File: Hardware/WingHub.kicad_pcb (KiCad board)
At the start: 2 copper layers, 50.8 x 22.9 mm, 19 parts, among them J1 feather long, J2 feather short, J3 USB_A, SW2 DOWNLOADER, U1 CH559T

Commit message: add model USB 3D
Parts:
- removed the J3 at (39.1, 33.3) (x2)
- removed the SW2 at (66.0, 33.3) (x2)
- added J3 (x2): USB_A, Connector_USB:USB_A_CONNFLY_DS1095-WNR0, F.Cu at (39.1, 33.3)
- added SW2 (x2): DOWNLOADER, Button_Switch_SMD:SW_SPST_TL3342, F.Cu at (66.0, 33.3)
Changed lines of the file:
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@@
     (tracks 182)
     (zones 0)
-    (modules 17)
+    (modules 19)
     (nets 42)
   )
@@
     (pad 5 thru_hole circle (at 10.07 2.71 270) (size 3.5 3.5) (drill 2.3) (layers *.Cu *.Mask)
       (net 6 "Net-(J3-Pad5)"))
-    (model ${KISYS3DMOD}/Connector_USB.3dshapes/USB_A_CONNFLY_DS1095-WNR0.wrl
-      (at (xyz 0 0 0))
+    (model ${KIPRJMOD}/femaleThruHoleUSB.stp
+      (offset (xyz 3.5 -12.5 4))
       (scale (xyz 1 1 1))
       (rotate (xyz 0 0 0))

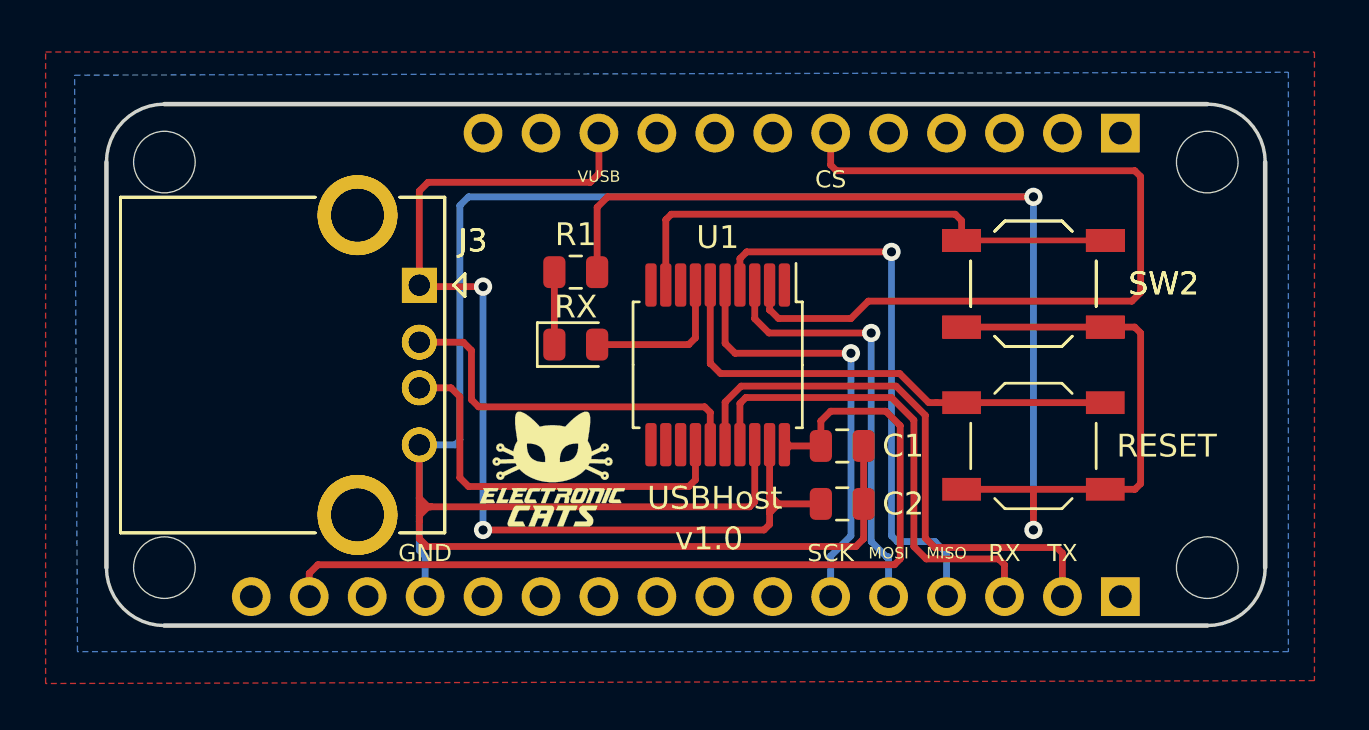
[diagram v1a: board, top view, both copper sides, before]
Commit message: fix labels pinout
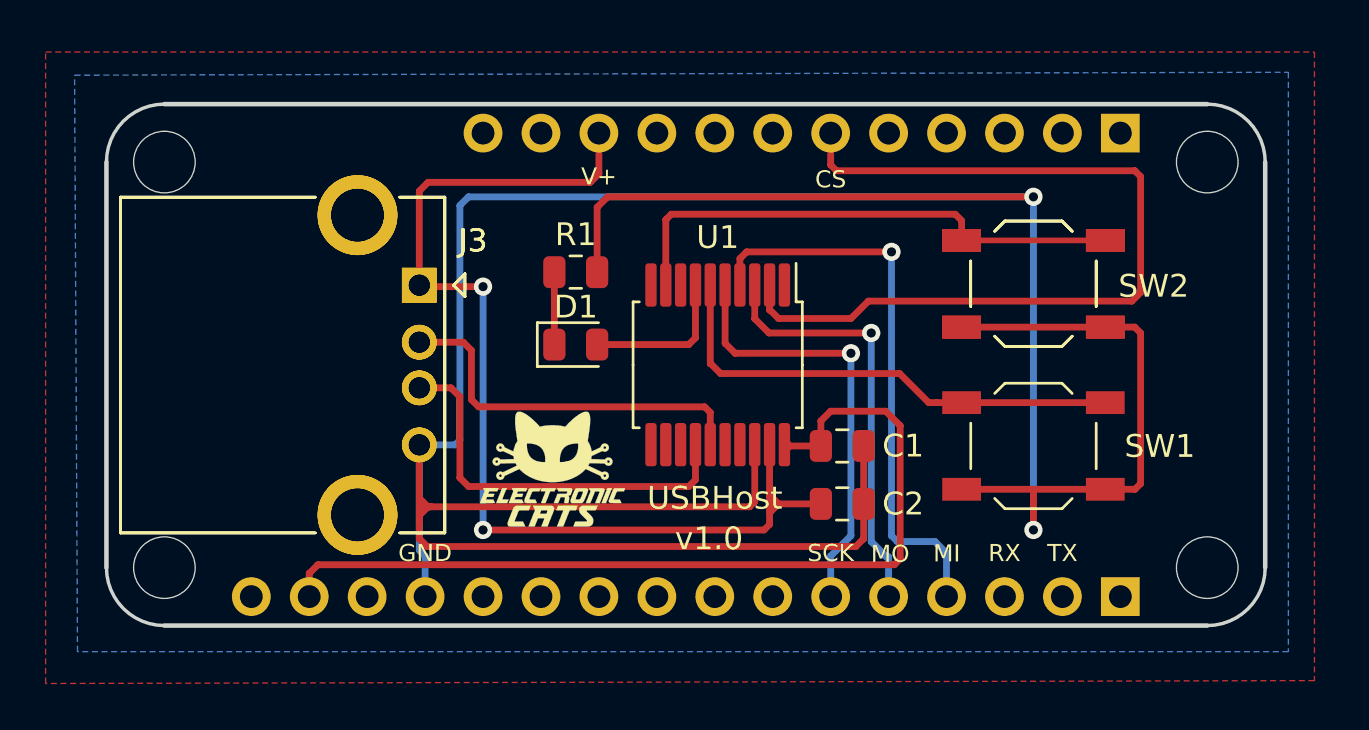
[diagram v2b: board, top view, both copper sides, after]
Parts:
- removed the J3 at (39.1, 33.3) (x2)
- removed the SW2 at (66.0, 33.3) (x2)
- added J3 (x2): USB_A, Connector_USB:USB_A_CONNFLY_DS1095-WNR0, F.Cu at (39.1, 33.3)
- added SW2 (x2): DOWNLOADER, Button_Switch_SMD:SW_SPST_TL3342, F.Cu at (66.0, 33.3)
- renumbered RX to D1, RESET to SW1
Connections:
- U1 pad 16: /TX -> /RX
- U1 pad 17: /RX -> /TX
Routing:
- net /TX: track 25.1 -> 0.00 mm
- net /RX: track 21.2 -> 0.00 mm
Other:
- board text added: "MI"
- board text added: "MO"
- board text added: "V+"
- board text removed: "MISO"
- board text removed: "MOSI"
- board text removed: "VUSB"
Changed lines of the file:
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@@
     (thickness 1.6)
     (drawings 25)
-    (tracks 182)
+    (tracks 162)
     (zones 0)
     (modules 19)
@@
     (38 B.Mask user)
     (39 F.Mask user)
-    (40 Dwgs.User user hide)
+    (40 Dwgs.User user)
     (41 Cmts.User user)
     (42 Eco1.User user)
@@
     (46 B.CrtYd user)
     (47 F.CrtYd user)
-    (48 B.Fab user hide)
-    (49 F.Fab user hide)
+    (48 B.Fab user)
+    (49 F.Fab user)
   )
   (setup
@@
     (tags "SPST Tactile Switch")
     (attr smd)
-    (fp_text reference SW2 (at 5.715 0 180) (layer F.SilkS)
+    (fp_text reference SW2 (at 5.27 0.106 180) (layer F.SilkS)
       (effects (font (size 1 1) (thickness 0.15)))
     )
@@
     (tags diode)
     (attr smd)
-    (fp_text reference RX (at 0 -1.65) (layer F.SilkS)
+    (fp_text reference D1 (at 0 -1.65) (layer F.SilkS)
       (effects (font (size 1 1) (thickness 0.15)))
     )
@@
       (net 3 GND))
     (pad 17 smd roundrect (at 3.5 -0.975 270) (size 1.9 0.5) (layers F.Cu F.Paste F.Mask) (roundrect_rratio 0.25)
+      (net 1 /TX))
+    (pad 16 smd roundrect (at 3.5 -0.325 270) (size 1.9 0.5) (layers F.Cu F.Paste F.Mask) (roundrect_rratio 0.25)
       (net 2 /RX))
-    (pad 16 smd roundrect (at 3.5 -0.325 270) (size 1.9 0.5) (layers F.Cu F.Paste F.Mask) (roundrect_rratio 0.25)
-      (net 1 /TX))
     (pad 15 smd roundrect (at 3.5 0.325 270) (size 1.9 0.5) (layers F.Cu F.Paste F.Mask) (roundrect_rratio 0.25)
       (net 33 /D-))
@@
     (tags "SPST Tactile Switch")
     (attr smd)
-    (fp_text reference SW2 (at 5.715 0 180) (layer F.SilkS)
+    (fp_text reference SW2 (at 6.39 -1.274 180) (layer F.Fab)
       (effects (font (size 1 1) (thickness 0.15)))
     )
@@
     (tags "SPST Tactile Switch")
     (attr smd)
-    (fp_text reference RESET (at 5.842 0 180) (layer F.SilkS)
+    (fp_text reference SW1 (at 5.54 0.014 180) (layer F.SilkS)
       (effects (font (size 1 1) (thickness 0.15)))
     )
@@
   (gr_line (start 55.88 22.86) (end 55.88 50.8) (layer F.Fab) (width 0.15))
   (gr_line (start 18.415 36.83) (end 80.01 36.83) (layer F.Fab) (width 0.15))
-  (gr_text VUSB (at 46.99 28.575) (layer F.SilkS)
-    (effects (font (size 0.5 0.5) (thickness 0.1)))
+  (gr_text V+ (at 46.99 28.575) (layer F.SilkS)
+    (effects (font (size 0.75 0.75) (thickness 0.15)))
   )
   (gr_text TX (at 67.31 45.085) (layer F.SilkS)
@@
     (effects (font (size 0.75 0.75) (thickness 0.15)))
   )
-  (gr_text MISO (at 62.23 45.085) (layer F.SilkS)
-    (effects (font (size 0.5 0.5) (thickness 0.1)))
-  )
-  (gr_text MOSI (at 59.69 45.085) (layer F.SilkS)
-    (effects (font (size 0.5 0.5) (thickness 0.1)))
+  (gr_text MI (at 62.24 45.1) (layer F.SilkS)
+    (effects (font (size 0.75 0.75) (thickness 0.15)))
+  )
+  (gr_text MO (at 59.76 45.12) (layer F.SilkS)
+    (effects (font (size 0.75 0.75) (thickness 0.15)))
   )
   (gr_text SCK (at 57.15 45.085) (layer F.SilkS)
@@
   (gr_line (start 76.2 27.94) (end 76.2 45.72) (layer Edge.Cuts) (width 0.2))
   (gr_line (start 27.94 25.4) (end 73.66 25.4) (layer Edge.Cuts) (width 0.2))
-  (segment (start 52.59699 40.25501) (end 52.522 40.33) (width 0.25) (layer F.Cu) (net 1))
-  (segment (start 67.31 45.212) (end 67.31 46.99) (width 0.3) (layer F.Cu) (net 1))
-  (segment (start 67.31 45.085) (end 67.31 45.212) (width 0.3) (layer F.Cu) (net 1))
-  (segment (start 61.71401 44.83899) (end 67.06399 44.83899) (width 0.3) (layer F.Cu) (net 1))
-  (segment (start 52.522 40.33) (end 52.522 38.46488) (width 0.3) (layer F.Cu) (net 1))
-  (segment (start 53.2249 37.76198) (end 60.018642 37.76198) (width 0.3) (layer F.Cu) (net 1))
-  (segment (start 67.06399 44.83899) (end 67.31 45.085) (width 0.3) (layer F.Cu) (net 1))
-  (segment (start 60.018642 37.76198) (end 61.298018 39.041358) (width 0.3) (layer F.Cu) (net 1))
-  (segment (start 52.522 38.46488) (end 53.2249 37.76198) (width 0.3) (layer F.Cu) (net 1))
-  (segment (start 61.298018 39.041358) (end 61.298018 44.422998) (width 0.3) (layer F.Cu) (net 1))
-  (segment (start 61.298018 44.422998) (end 61.71401 44.83899) (width 0.3) (layer F.Cu) (net 1))
-  (segment (start 64.77 45.593) (end 64.77 46.99) (width 0.3) (layer F.Cu) (net 2))
-  (segment (start 64.516 45.339) (end 64.77 45.593) (width 0.3) (layer F.Cu) (net 2))
-  (segment (start 61.341 45.339) (end 64.516 45.339) (width 0.3) (layer F.Cu) (net 2))
-  (segment (start 53.172 40.33) (end 53.172 38.522) (width 0.3) (layer F.Cu) (net 2))
-  (segment (start 53.172 38.522) (end 53.43201 38.26199) (width 0.3) (layer F.Cu) (net 2))
-  (segment (start 60.79801 44.79601) (end 61.341 45.339) (width 0.3) (layer F.Cu) (net 2))
-  (segment (start 53.43201 38.26199) (end 59.811532 38.26199) (width 0.3) (layer F.Cu) (net 2))
-  (segment (start 59.811532 38.26199) (end 60.798009 39.248467) (width 0.3) (layer F.Cu) (net 2))
-  (segment (start 60.798009 39.248467) (end 60.79801 44.79601) (width 0.3) (layer F.Cu) (net 2))
   (segment (start 39.116 46.736) (end 39.37 46.99) (width 0.5) (layer B.Cu) (net 3))
   (segment (start 58.5955 40.386) (end 58.5955 42.418) (width 0.3) (layer F.Cu) (net 3))
@@
     (connect_pads (clearance 0.508))
     (min_thickness 0.254)
-    (fill yes (arc_segments 32) (thermal_gap 0.508) (thermal_bridge_width 0.508))
+    (fill (arc_segments 32) (thermal_gap 0.508) (thermal_bridge_width 0.508))
     (polygon
       (pts
@@
     (connect_pads (clearance 0.508))
     (min_thickness 0.254)
-    (fill yes (arc_segments 32) (thermal_gap 0.508) (thermal_bridge_width 0.508))
+    (fill (arc_segments 32) (thermal_gap 0.508) (thermal_bridge_width 0.508))
     (polygon
       (pts

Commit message: Tx and Rx routes exchanged.
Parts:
- removed the J3 at (39.1, 33.3) (x2)
- removed the SW2 at (66.0, 33.3) (x2)
- added J3 (x2): USB_A, Connector_USB:USB_A_CONNFLY_DS1095-WNR0, F.Cu at (39.1, 33.3)
- added SW2 (x2): DOWNLOADER, Button_Switch_SMD:SW_SPST_TL3342, F.Cu at (66.0, 33.3)
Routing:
- net /RX: track 0.00 -> 23.8 mm
- net /TX: track 0.00 -> 23.6 mm, vias 0 -> 1

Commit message: labels buttons
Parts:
- removed the J3 at (39.1, 33.3) (x2)
- removed the SW2 at (66.0, 33.3) (x2)
- added J3 (x2): USB_A, Connector_USB:USB_A_CONNFLY_DS1095-WNR0, F.Cu at (39.1, 33.3)
- added PROG, SW2: DOWNLOADER, Button_Switch_SMD:SW_SPST_TL3342, F.Cu at (66.0, 33.3)
- renumbered SW1 to RESET
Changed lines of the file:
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@@
-(kicad_pcb (version 20171130) (host pcbnew 5.1.6-c6e7f7d~86~ubuntu18.04.1)
+(kicad_pcb (version 20171130) (host pcbnew "(5.1.5-0-10_14)")
   (general
     (thickness 1.6)
@@
     (tags "SPST Tactile Switch")
     (attr smd)
-    (fp_text reference SW2 (at 5.27 0.106 180) (layer F.SilkS)
+    (fp_text reference PROG (at 5.27 0.106 180) (layer F.SilkS)
       (effects (font (size 1 1) (thickness 0.15)))
     )
@@
     (tags "SPST Tactile Switch")
     (attr smd)
-    (fp_text reference SW1 (at 5.54 0.014 180) (layer F.SilkS)
+    (fp_text reference RESET (at 5.54 0.014 180) (layer F.SilkS)
       (effects (font (size 1 1) (thickness 0.15)))
     )

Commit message: WingHubBom.ods created with plugin.
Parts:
- removed the J3 at (39.1, 33.3) (x2)
- added J3 (x2): USB_A, Connector_USB:USB_A_CONNFLY_DS1095-WNR0, F.Cu at (39.1, 33.3)

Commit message: Hardware changes added
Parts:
- removed the J3 at (39.1, 33.3) (x2)
- removed SW2: DOWNLOADER, Button_Switch_SMD:SW_SPST_TL3342
- added J3 (x2): USB_A, Connector_USB:USB_A_CONNFLY_DS1095-WNR0, F.Cu at (39.1, 33.3)
- moved R1 18.5 mm to (63.4, 38.9), turned to 180 degrees
- moved D1 17.4 mm to (63.4, 36.8), turned to 180 degrees
- moved RESET 4.53 mm to (70.5, 40.0)
- moved PROG 4.52 mm to (70.5, 33.7)
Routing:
- net GND: track 152.6 -> 130.3 mm
- net /RST: track 22.4 -> 34.6 mm, vias 0 -> 2
- net /CS: track 38.3 -> 47.1 mm
- net /LED: track 6.75 -> 15.2 mm
- net /PROG: track 24.3 -> 29.2 mm
- net Net-(D1-Pad1): track 3.18 -> 2.08 mm
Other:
- board text added: "3V3"
